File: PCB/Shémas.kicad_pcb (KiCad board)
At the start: 4 copper layers, 65 x 26 mm, 44 parts, among them J1 Conn_01x04_Socket, J3 Conn_01x04_Socket, J4 Conn_01x03_Socket, U1 MCP3221, U2 TCA9517, U3 XIAO ESP32C3, U5 LM117_TO3, U6 TJA1051T, U7 LM2674M-5.0

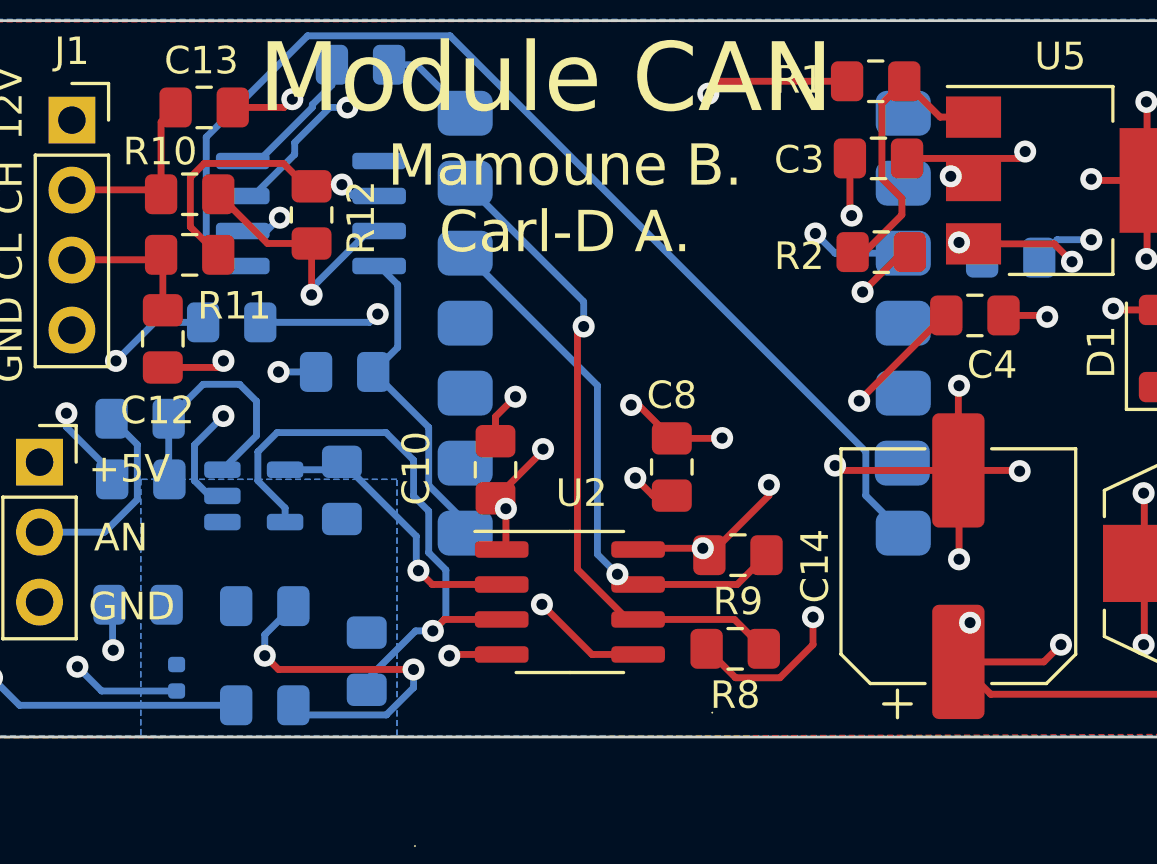
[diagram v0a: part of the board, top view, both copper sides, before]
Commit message: Correction du pcb
changemnet blm en 0603 et rx-rx et tx-tx
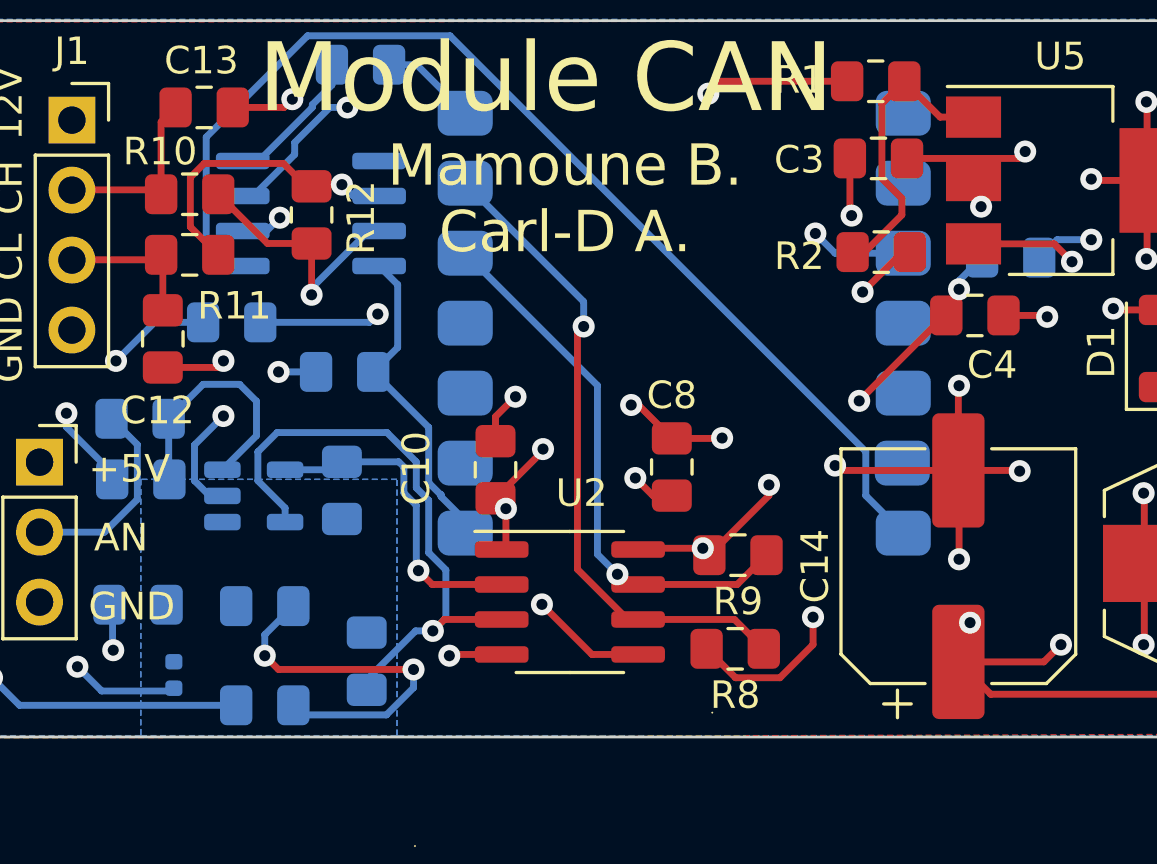
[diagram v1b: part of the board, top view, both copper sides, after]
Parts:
- moved FB1 0.14 mm to (102.2, 85.1)
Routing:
- net /SCLA: track 10.5 -> 11.7 mm
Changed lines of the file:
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@@
   )
   (footprint "Capacitor_SMD:C_0402_1005Metric" (layer "B.Cu")
-    (at 102.3 85.2 90)
+    (at 102.2 85.1 90)
     (descr "Capacitor SMD 0402 (1005 Metric), square (rectangular) end terminal, IPC_7351 nominal, (Body size source: IPC-SM-782 page 76, https://www.pcb-3d.com/wordpress/wp-content/uploads/ipc-sm-782a_amendment_1_and_2.pdf), generated with kicad-footprint-generator")
     (tags "capacitor")
@@
   (segment (start 139.75 67.15) (end 139.8 67.1) (width 0.25) (layer "F.Cu") (net 3))
   (segment (start 128.8125 66.35) (end 132.85 66.35) (width 0.25) (layer "F.Cu") (net 3))
-  (segment (start 131.225 67.15) (end 131.075 67) (width 0.25) (layer "F.Cu") (net 3))
   (segment (start 137.425 81.05) (end 137.425 78.525) (width 0.25) (layer "F.Cu") (net 3))
   (segment (start 130.675 84.625) (end 133.775 84.625) (width 0.25) (layer "F.Cu") (net 3))
@@
   (segment (start 137.525 67.15) (end 137.525 69.975) (width 0.25) (layer "F.Cu") (net 3))
   (segment (start 130.675 84.625) (end 131.1 84.2) (width 0.25) (layer "F.Cu") (net 3))
+  (segment (start 131.5 67.425) (end 131.225 67.15) (width 0.25) (layer "F.Cu") (net 3))
   (segment (start 137.525 64.325) (end 137.5 64.3) (width 0.25) (layer "F.Cu") (net 3))
   (segment (start 117.378094 84.355) (end 119.05 84.355) (width 0.25) (layer "F.Cu") (net 3))
@@
   (segment (start 115.560099 82.537005) (end 117.378094 84.355) (width 0.25) (layer "F.Cu") (net 3))
   (segment (start 137.425 83.975) (end 137.4 84) (width 0.25) (layer "F.Cu") (net 3))
-  (segment (start 131.075 67) (end 130.4 67) (width 0.25) (layer "F.Cu") (net 3))
   (segment (start 137.425 81.05) (end 137.425 83.975) (width 0.25) (layer "F.Cu") (net 3))
+  (segment (start 131.5 68.100498) (end 131.5 67.425) (width 0.25) (layer "F.Cu") (net 3))
   (via (at 115.560099 82.537005) (size 0.8) (drill 0.4) (layers "F.Cu" "B.Cu") (net 3))
   (via (at 147.8 70.3) (size 0.8) (drill 0.4) (layers "F.Cu" "B.Cu") (net 3))
-  (via (at 130.4 67) (size 0.8) (drill 0.4) (layers "F.Cu" "B.Cu") (net 3))
+  (via (at 131.5 68.100498) (size 0.8) (drill 0.4) (layers "F.Cu" "B.Cu") (net 3))
   (via (at 140.4 81.1) (size 0.8) (drill 0.4) (layers "F.Cu" "B.Cu") (net 3))
   (via (at 139.8 67.1) (size 0.8) (drill 0.4) (layers "F.Cu" "B.Cu") (net 3))
@@
   (via (at 127.0755 75.150528) (size 0.8) (drill 0.4) (layers "F.Cu" "B.Cu") (net 5))
   (via (at 121.4 80.5) (size 0.8) (drill 0.4) (layers "F.Cu" "B.Cu") (net 5))
-  (via (at 130.7 69.4) (size 0.8) (drill 0.4) (layers "F.Cu" "B.Cu") (net 5))
+  (via (at 130.7 71.1) (size 0.8) (drill 0.4) (layers "F.Cu" "B.Cu") (net 5))
   (via (at 127.2 71.2) (size 0.8) (drill 0.4) (layers "F.Cu" "B.Cu") (net 5))
   (via (at 125.485133 69.074444) (size 0.8) (drill 0.4) (layers "F.Cu" "B.Cu") (net 5))
-  (segment (start 131.5375 69.95) (end 130.9875 69.4) (width 0.25) (layer "B.Cu") (net 5))
-  (segment (start 130.9875 69.4) (end 130.7 69.4) (width 0.25) (layer "B.Cu") (net 5))
+  (segment (start 130.7 70.7875) (end 130.7 71.1) (width 0.25) (layer "B.Cu") (net 5))
   (segment (start 128.675 69.79) (end 126.200689 69.79) (width 0.25) (layer "B.Cu") (net 5))
   (segment (start 126.200689 69.79) (end 125.485133 69.074444) (width 0.25) (layer "B.Cu") (net 5))
+  (segment (start 131.5375 69.95) (end 130.7 70.7875) (width 0.25) (layer "B.Cu") (net 5))
   (segment (start 102.0125 75.8) (end 102.0125 77.975) (width 0.25) (layer "B.Cu") (net 6))
   (segment (start 103.2625 74.55) (end 102.0125 75.8) (width 0.25) (layer "B.Cu") (net 6))
@@
   (segment (start 111.57949 81.815) (end 114.1 81.815) (width 0.25) (layer "F.Cu") (net 11))
   (via (at 111.077051 81.312561) (size 0.8) (drill 0.4) (layers "F.Cu" "B.Cu") (net 11))
-  (segment (start 106.2375 77.65) (end 108.0125 77.65) (width 0.25) (layer "B.Cu") (net 11))
   (segment (start 111.077051 81.312561) (end 111 81.23551) (width 0.25) (layer "B.Cu") (net 11))
+  (segment (start 106.2375 77.65) (end 108.0125 77.65) (width 0.25) (layer "B.Cu") (net 11))
+  (segment (start 111 78.943703) (end 110.55 78.493703) (width 0.25) (layer "B.Cu") (net 11))
   (segment (start 108.0125 77.65) (end 108.3 77.3625) (width 0.25) (layer "B.Cu") (net 11))
-  (segment (start 111 80.0625) (end 108.3 77.3625) (width 0.25) (layer "B.Cu") (net 11))
-  (segment (start 111 81.23551) (end 111 80.0625) (width 0.25) (layer "B.Cu") (net 11))
+  (segment (start 111 81.23551) (end 111 78.943703) (width 0.25) (layer "B.Cu") (net 11))
+  (segment (start 110.55 78.493703) (end 110.55 77.55) (width 0.25) (layer "B.Cu") (net 11))
+  (segment (start 110.3625 77.3625) (end 108.3 77.3625) (width 0.25) (layer "B.Cu") (net 11))
+  (segment (start 110.55 77.55) (end 110.3625 77.3625) (width 0.25) (layer "B.Cu") (net 11))
   (segment (start 114.1 83.085) (end 112.015 83.085) (width 0.25) (layer "F.Cu") (net 12))
   (segment (start 112.015 83.085) (end 111.6 83.5) (width 0.25) (layer "F.Cu") (net 12))
   (via (at 111.6 83.5) (size 0.8) (drill 0.4) (layers "F.Cu" "B.Cu") (net 12))
-  (segment (start 110.9 78.6) (end 110.9 77.3) (width 0.25) (layer "B.Cu") (net 12))
-  (segment (start 112.075 83.025) (end 112.075 81.285911) (width 0.25) (layer "B.Cu") (net 12))
-  (segment (start 110.9 77.3) (end 109.9 76.3) (width 0.25) (layer "B.Cu") (net 12))
-  (segment (start 112.075 81.285911) (end 111.45 80.660911) (width 0.25) (layer "B.Cu") (net 12))
-  (segment (start 110.974695 83.5) (end 111.6 83.5) (width 0.25) (layer "B.Cu") (net 12))
+  (segment (start 111.45 80.660911) (end 111.45 78.757307) (width 0.25) (layer "B.Cu") (net 12))
+  (segment (start 109.936396 76.3) (end 105.948896 76.3) (width 0.25) (layer "B.Cu") (net 12))
   (segment (start 106.2375 79.0375) (end 106.2375 79.55) (width 0.25) (layer "B.Cu") (net 12))
-  (segment (start 109.2 85.274695) (end 110.974695 83.5) (width 0.25) (layer "B.Cu") (net 12))
+  (segment (start 111 77.363604) (end 109.936396 76.3) (width 0.25) (layer "B.Cu") (net 12))
   (segment (start 105.948896 76.3) (end 105.25 76.998896) (width 0.25) (layer "B.Cu") (net 12))
   (segment (start 111.6 83.5) (end 112.075 83.025) (width 0.25) (layer "B.Cu") (net 12))
-  (segment (start 111.45 80.660911) (end 111.45 79.15) (width 0.25) (layer "B.Cu") (net 12))
-  (segment (start 111.45 79.15) (end 110.9 78.6) (width 0.25) (layer "B.Cu") (net 12))
-  (segment (start 109.9 76.3) (end 105.948896 76.3) (width 0.25) (layer "B.Cu") (net 12))
-  (segment (start 105.25 76.998896) (end 105.25 78.05) (width 0.25) (layer "B.Cu") (net 12))
+  (segment (start 110.974695 83.5) (end 111.6 83.5) (width 0.25) (layer "B.Cu") (net 12))
+  (segment (start 111 78.307307) (end 111 77.363604) (width 0.25) (layer "B.Cu") (net 12))
+  (segment (start 112.075 81.285911) (end 111.45 80.660911) (width 0.25) (layer "B.Cu") (net 12))
+  (segment (start 109.2 85.274695) (end 110.974695 83.5) (width 0.25) (layer "B.Cu") (net 12))
+  (segment (start 112.075 83.025) (end 112.075 81.285911) (width 0.25) (layer "B.Cu") (net 12))
+  (segment (start 111.45 78.757307) (end 111 78.307307) (width 0.25) (layer "B.Cu") (net 12))
   (segment (start 109.2 85.6375) (end 109.2 85.274695) (width 0.25) (layer "B.Cu") (net 12))
+  (segment (start 105.25 76.998896) (end 105.25 78.05) (width 0.25) (layer "B.Cu") (net 12))
   (segment (start 105.25 78.05) (end 106.2375 79.0375) (width 0.25) (layer "B.Cu") (net 12))
   (segment (start 107.225 64.400305) (end 107.9375 63.687805) (width 0.25) (layer "B.Cu") (net 13))
@@
   (segment (start 110.0125 62.95) (end 111.015 62.95) (width 0.25) (layer "B.Cu") (net 14))
   (segment (start 111.015 62.95) (end 112.775 64.71) (width 0.25) (layer "B.Cu") (net 14))
-  (segment (start 112.775 79.95) (end 112.775 79.538604) (width 0.25) (layer "B.Cu") (net 15))
+  (segment (start 111.9 78.55) (end 111.879089 78.55) (width 0.25) (layer "B.Cu") (net 15))
   (segment (start 110.325 73.2125) (end 110.325 70.93) (width 0.25) (layer "B.Cu") (net 15))
-  (segment (start 110.325 70.93) (end 109.65 70.255) (width 0.25) (layer "B.Cu") (net 15))
-  (segment (start 111.45 78.213604) (end 111.45 76.1125) (width 0.25) (layer "B.Cu") (net 15))
-  (segment (start 112.775 79.538604) (end 111.45 78.213604) (width 0.25) (layer "B.Cu") (net 15))
+  (segment (start 112.775 79.502208) (end 111.9 78.627208) (width 0.25) (layer "B.Cu") (net 15))
   (segment (start 111.45 76.1125) (end 109.4375 74.1) (width 0.25) (layer "B.Cu") (net 15))
+  (segment (start 112.775 79.95) (end 112.775 79.502208) (width 0.25) (layer "B.Cu") (net 15))
+  (segment (start 110.325 70.93) (end 109.65 70.255) (width 0.25) (layer "B.Cu") (net 15))
+  (segment (start 111.45 78.120911) (end 111.45 76.1125) (width 0.25) (layer "B.Cu") (net 15))
   (segment (start 109.4375 74.1) (end 110.325 73.2125) (width 0.25) (layer "B.Cu") (net 15))
+  (segment (start 111.879089 78.55) (end 111.45 78.120911) (width 0.25) (layer "B.Cu") (net 15))
+  (segment (start 111.9 78.627208) (end 111.9 78.55) (width 0.25) (layer "B.Cu") (net 15))
   (segment (start 118.673249 83.085) (end 119.05 83.085) (width 0.25) (layer "F.Cu") (net 16))
   (segment (start 116.85 81.261751) (end 118.673249 83.085) (width 0.25) (layer "F.Cu") (net 16))
